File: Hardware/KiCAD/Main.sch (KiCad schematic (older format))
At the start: 4 parts

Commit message: More work on the schematic
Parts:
- added C?: C, symbol C
- added IC?: MAX3232_BJH, maxim-DIL16, symbol MAX3232_BJH
- added J?: ICSP, symbol CONN_01X06
- added J?: DB9, symbol DB9
- added JP?: Jumper, symbol Jumper
- added R?: 10K, symbol R
- added R? (x2): 220, symbol R
- added U?: POXA1328-007, symbol POXA1328-007
- added U?: 4000series-4052, DIP16, symbol 4000series-4052
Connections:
- net GND: now also J?.3 (P3), J?.5, JP?.2, U?.6 (INH)
- net PGC: now also J?.5 (P5)
- net PGD: now also J?.4 (P4)
- net RX2: now also R?.1
- net RX4: now also J?.3
- net S1: now also U?.10 (A)
- net S2: now also U?.9 (B)
- net TX2: now also R?.1
- net TX4: now also J?.2
- net ~MCLR: now reaches U?.1 (RE3/~MCLR)
- net ~MCLR: now also C?.1, J?.1 (P1), R?.2
- new net: C?.2, JP?.1
- new net: R?.2, U?.10 (RX)
- new net: R?.2, U?.9 (TX)
- new net +3.3V: J?.2 (P2), R?.1
- new net 1PPS: U?.6 (1PPS)
- new net DSR1: U?.1 (Y0)
- new net DSR2: U?.5 (Y1)
- new net DSR3: U?.2 (Y2)
- new net DSR4: U?.4 (Y3)
- new net DTR: U?.3 (Y_COM)
- new net DTR1: U?.12 (X0)
- new net DTR2: U?.14 (X1)
- new net DTR3: U?.15 (X2)
- new net DTR4: U?.11 (X3)
- new net DTS: U?.13 (X_COM)
- new net FIX: U?.5 (3D-FIX)
- no-connect marks 5 -> 12
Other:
- moved on the sheet: U?A

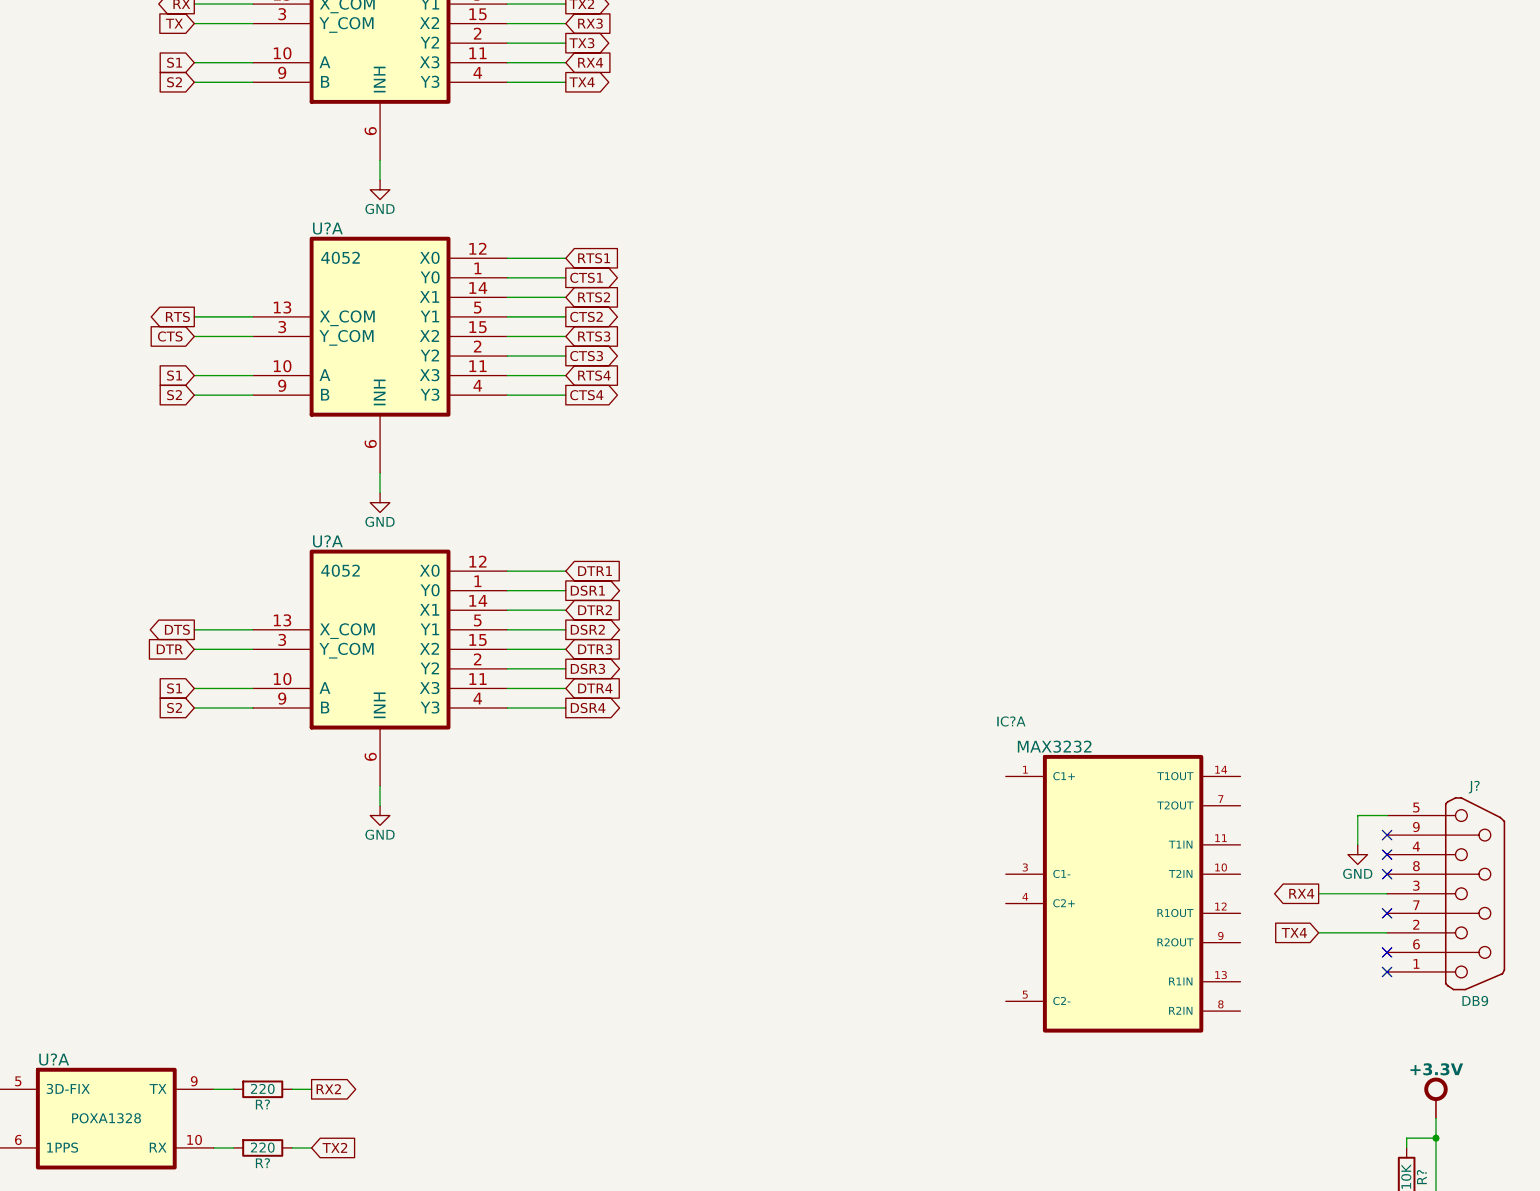
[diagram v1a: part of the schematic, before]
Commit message: Pretty much finished the RS232 side of things
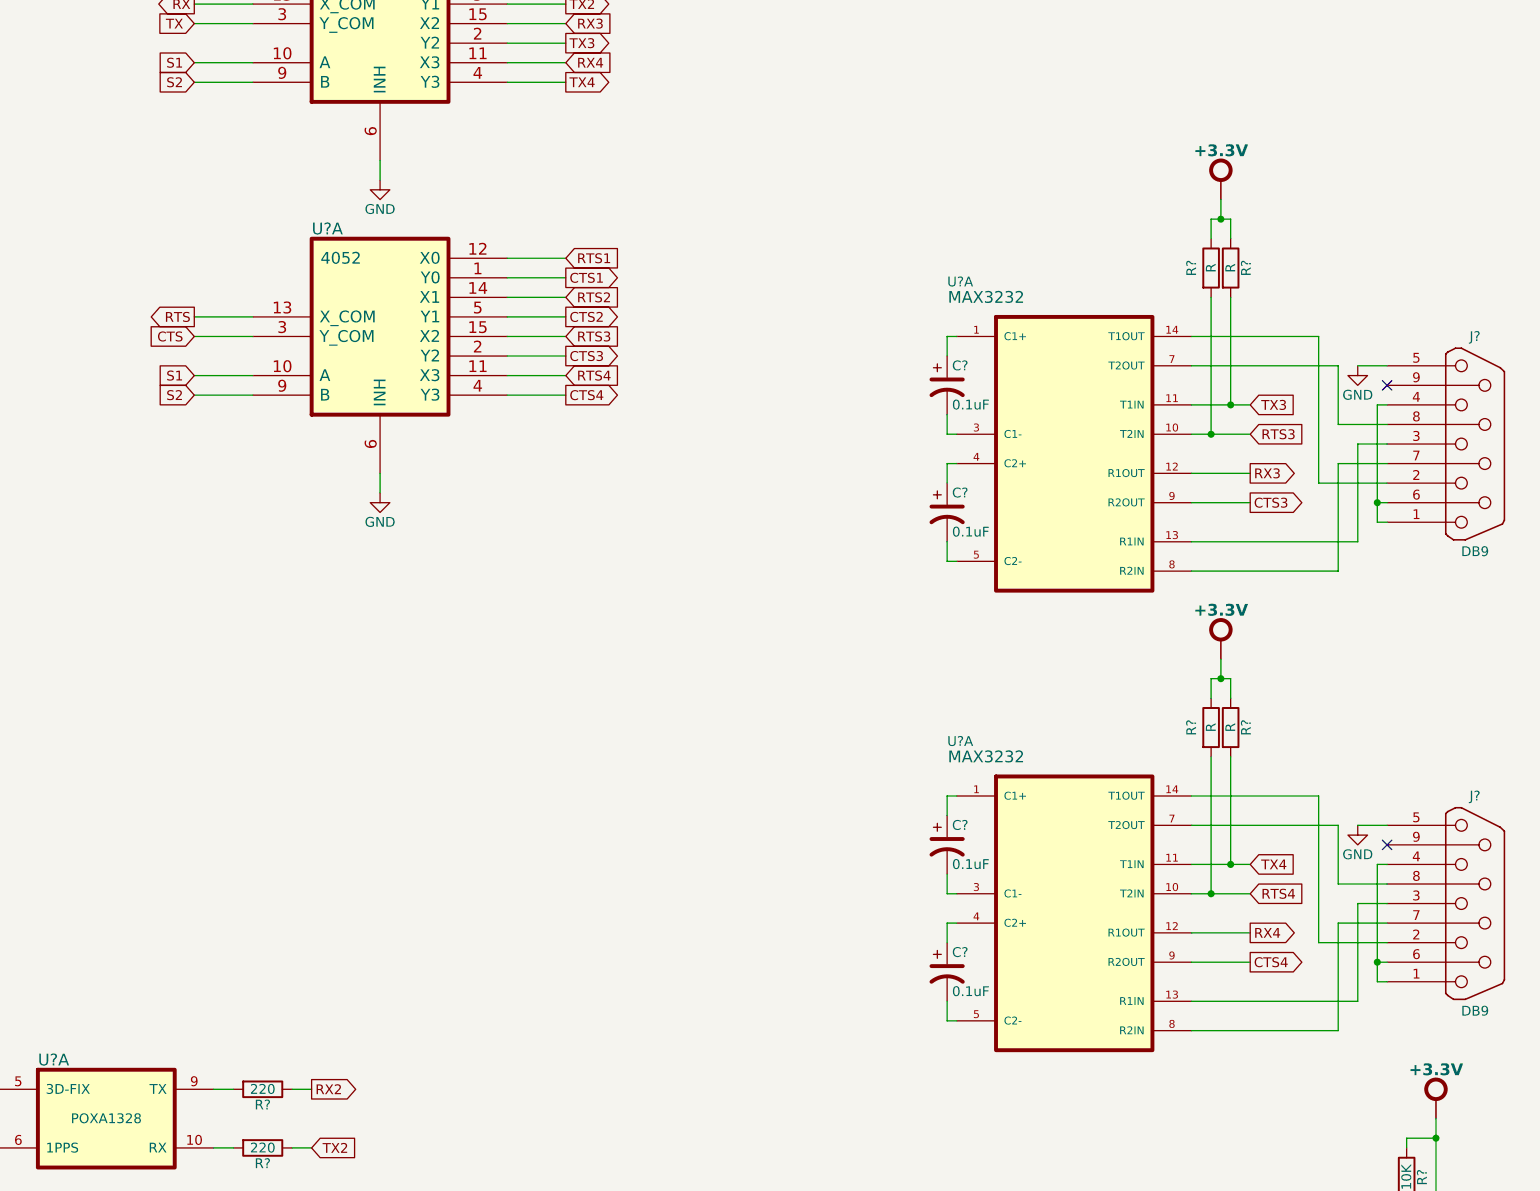
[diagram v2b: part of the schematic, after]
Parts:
- removed IC?: MAX3232_BJH, maxim-DIL16, symbol MAX3232_BJH
- removed J?: DB9, symbol DB9
- removed U?: 4000series-4052, DIP16, symbol 4000series-4052
- added C? (x4): 0.1uF, symbol CP1
- added J? (x2): DB9, symbol DB9
- added R? (x4): R, symbol R
- added U? (x2): MAX3232_BJH, maxim-DIL16, symbol MAX3232_BJH
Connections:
- net +3.3V: now also R?.1, R?.1, R?.1, R?.1
- net CTS3: now also U?.9 (R2OUT)
- net CTS4: now also U?.9 (R2OUT)
- net GND: now also J?.5, J?.5
- net RTS3: now also R?.2, U?.10 (T2IN)
- net RTS4: now also R?.2, U?.10 (T2IN)
- net RX3: now also U?.12 (R1OUT)
- net RX4: now also U?.12 (R1OUT)
- net TX3: now also R?.2, U?.11 (T1IN)
- net TX4: now also R?.2, U?.11 (T1IN)
- new net: J?.1, J?.4, J?.6 (P6) (x2)
- new net: J?.2, U?.14 (T1OUT) (x2)
- new net: J?.3, U?.13 (R1IN) (x2)
- new net: J?.7 (P7), U?.8 (R2IN) (x2)
- new net: J?.8 (P8), U?.7 (T2OUT) (x2)
- new net: C?.1, U?.1 (C1+) (x2)
- new net: C?.2, U?.3 (C1-) (x2)
- new net: C?.1, U?.4 (C2+) (x2)
- new net: C?.2, U?.5 (C2-) (x2)
- no-connect marks 12 -> 8

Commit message: More work on the schematic
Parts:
- added C?: 12pF, symbol C_Small
- added C?: 10pF, symbol C_Small
- added R?: 10K, symbol R
- added U?: MCP795XX, symbol MCP795XX
- added Y?: 32.768Hz, symbol Crystal
- added Y?: 12MHz, symbol Crystal
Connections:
- net +3.3V: now also R?.1
- net at U?.10 (RA6/OSC2/CLKout): now also Y?.2
- net SCLK: now reaches U?.14 (RC3/SCK/SCL)
- net SCLK: now also U?.8 (SCK)
- net MSDI: now reaches U?.15 (SDA/SDI/RC4)
- net MSDI: now also U?.7 (SO)
- net MSDO: now reaches U?.16 (SDO/RC5)
- net MSDO: now also U?.6 (SI)
- net RTC_SS: now reaches U?.21 (AN10/RB0)
- net RTC_SS: now also U?.3 (~CS)
- net ALARM: now reaches U?.22 (AN8/INT1/RB1)
- net ALARM: now also R?.2, U?.9 (MFP)
- net FLASH_SS: now reaches U?.26 (RB5)
- net at U?.9 (RA7/OSC1/CLKin): now also Y?.1
- new net: C?.1, U?.1 (X1), Y?.1
- new net: C?.1, U?.2 (X2), Y?.2
- new net: C?.2, C?.2
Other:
- moved on the sheet: C?, J?, JP?, R?, U?A

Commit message: more work on the schematic
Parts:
- added U?: S25FL127S_SOIC, symbol S25FL127S_SOIC
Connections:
- wire segments 166 -> 170
- no-connect marks 8 -> 11
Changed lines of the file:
@@
 LIBS:Relays
 LIBS:Transistors-BJH
+LIBS:MemoryDevices-BJH
 LIBS:ptws-cache
 EELAYER 25 0
@@
 Wire Wire Line
 	7350 5550 7350 5700
+$Comp
+L S25FL127S_SOIC U?
+U 1 1 57B9C014
+P 5850 4650
+F 0 "U?" H 5850 4700 60  0000 L CNN
+F 1 "S25FL127S_SOIC" H 5850 4800 60  0000 L CNN
+F 2 "" H 6200 4450 60  0000 C CNN
+F 3 "" H 6200 4450 60  0000 C CNN
+	1    5850 4650
+	1    0    0    -1
+$EndComp
+Text GLabel 5350 4750 0    50   Input ~ 0
+FLASH_SS
+Wire Wire Line
+	5350 4750 5650 4750
+Text GLabel 5350 4850 0    50   Input ~ 0
+SCLK
+Wire Wire Line
+	5350 4850 5650 4850
+Text GLabel 5350 5050 0    50   Input ~ 0
+MSDO
+Wire Wire Line
+	5350 5050 5650 5050
+Text GLabel 5350 4950 0    50   Output ~ 0
+MSDI
+Wire Wire Line
+	5350 4950 5650 4950
+NoConn ~ 7100 4850
+NoConn ~ 7100 4750
+NoConn ~ 7100 4950
 $EndSCHEMATC

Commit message: more work on PTWS schematic
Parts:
- U4: renamed from U?; symbol S25FL127S_SOIC -> S25FL127S_SOIC-RESCUE-ptws
- gave numbers to parts that had none: 29
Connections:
- wire segments 170 -> 171

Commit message: More work on PTWS
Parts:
- added C25, C26: C_Small, symbol C_Small
- added J4: SPARE, symbol CONN_01X02
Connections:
- net GND: now also C2.2, C3.2, C25.2, C26.1
- net at U1.10 (RA6/OSC2/CLKout), Y1.2: now also C26.2
- net at U1.24 (CANRX/INT3/RB3): now also J4.2 (P2)
- net at U1.25 (AN9/RB4): now also J4.1 (P1)
- net at U1.9 (RA7/OSC1/CLKin), Y1.1: now also C25.1
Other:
- moved on the sheet: Y1

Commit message: More work on PTWS schematic
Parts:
- removed C25, C26: C_Small, symbol C_Small
- removed J4: SPARE, symbol CONN_01X02
- removed Y1: 12MHz, symbol Crystal
- added TP?: CLK_OUT, symbol CONN_01X01
- R5, R7: value R -> 1K
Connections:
- net ACTIV_LED is gone; now on net BT_ACTIV: U3.12 (PIO3/MOSI/WS)
- net CONN_LED is gone; now on net BT_CONN: U3.10 (SCK/PIO1)
- net EVENT_LED is gone; now on net BT_MLDP_EV: U3.11 (PIO2/CS/MLDP_EV)
- net GND: now also C2.1; no longer C2.2
- net at U1.10 (RA6/OSC2/CLKout): now also TP?.1 (P1)
- net BT_MLDP_EV: now reaches U1.24 (CANRX/INT3/RB3)
- net BT_CONN: now reaches U1.25 (AN9/RB4)
- net BT_ACTIV: now reaches U1.9 (RA7/OSC1/CLKin)
- net at U7.1 (X1), Y2.1: now also C2.2; no longer C2.1
- net CTS2: no longer names the net of U6.5 (Y1)
- net MSDI renamed MISO
- net MSDO renamed MOSI
- net RTS2: no longer names the net of U6.14 (X1)
- no-connect marks 11 -> 14
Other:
- moved on the sheet: C2, C3, R2, R3, U1A, U2A, U3A, U4A, U5A, U6A

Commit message: more work on the schematic
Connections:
- no-connect marks 14 -> 13
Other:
- moved on the sheet: C2, C3
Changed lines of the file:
@@
 LIBS:Relays
 LIBS:Transistors-BJH
+LIBS:MemoryDevices-BJH
 LIBS:ptws-cache
 EELAYER 25 0
@@
 L C_Small C3
 U 1 1 57B87644
-P 7850 5950
-F 0 "C3" H 7800 6100 50  0000 L CNN
-F 1 "12pF" H 7700 6150 50  0000 L CNN
-F 2 "" H 7850 5950 50  0000 C CNN
-F 3 "" H 7850 5950 50  0000 C CNN
-	1    7850 5950
-	-1   0    0    1
-$EndComp
-$Comp
-L C_Small C2
-U 1 1 57B87717
-P 7850 5750
-F 0 "C2" V 7900 5600 50  0000 L CNN
-F 1 "10pF" V 8000 5600 50  0000 L CNN
-F 2 "" H 7850 5750 50  0000 C CNN
-F 3 "" H 7850 5750 50  0000 C CNN
-	1    7850 5750
+P 7850 6000
+F 0 "C3" H 7950 6000 50  0000 L CNN
+F 1 "12pF" H 7850 5900 50  0000 L CNN
+F 2 "" H 7850 6000 50  0000 C CNN
+F 3 "" H 7850 6000 50  0000 C CNN
+	1    7850 6000
 	-1   0    0    1
 $EndComp
@@
 L GND #PWR012
 U 1 1 58010C74
-P 7700 5950
-F 0 "#PWR012" H 7700 5700 50  0001 C CNN
-F 1 "GND" H 7700 5800 50  0000 C CNN
-F 2 "" H 7700 5950 50  0000 C CNN
-F 3 "" H 7700 5950 50  0000 C CNN
-	1    7700 5950
+P 7600 5950
+F 0 "#PWR012" H 7600 5700 50  0001 C CNN
+F 1 "GND" H 7600 5800 50  0000 C CNN
+F 2 "" H 7600 5950 50  0000 C CNN
+F 3 "" H 7600 5950 50  0000 C CNN
+	1    7600 5950
 	1    0    0    -1
 $EndComp
@@
 	9700 1400 9700 1950
 Wire Wire Line
-	9500 1950 9800 1950
-Wire Wire Line
-	9500 2100 9800 2100
+	9500 1950 9700 1950
+Wire Wire Line
+	9700 1950 9800 1950
+Wire Wire Line
+	9500 2100 9600 2100
+Wire Wire Line
+	9600 2100 9800 2100
 Wire Wire Line
 	10250 2050 10500 2050
@@
 	10450 1950 10500 1950
 Wire Wire Line
-	10450 1950 10450 2550
+	10450 1950 10450 2450
+Wire Wire Line
+	10450 2450 10450 2550
 Wire Wire Line
 	10450 2550 10500 2550
@@
 Connection ~ 1100 6350
 Wire Wire Line
-	1100 6250 1100 6850
+	1100 6250 1100 6350
+Wire Wire Line
+	1100 6350 1100 6850
 Connection ~ 950  5900
 Wire Wire Line
@@
 	950  6450 850  6450
 Wire Wire Line
-	950  5800 950  6450
+	950  5800 950  5900
+Wire Wire Line
+	950  5900 950  6450
 Wire Wire Line
 	1300 6750 850  6750
@@
 	1300 6650 850  6650
 Wire Wire Line
-	850  6350 1300 6350
+	850  6350 1100 6350
+Wire Wire Line
+	1100 6350 1300 6350
 Wire Wire Line
 	3350 3350 3700 3350
@@
 	9600 1100 9600 1000
 Wire Wire Line
-	9600 1000 9700 1000
+	9600 1000 9650 1000
+Wire Wire Line
+	9650 1000 9700 1000
 Wire Wire Line
 	9700 1000 9700 1100
@@
 	9700 3750 9700 4300
 Wire Wire Line
-	9500 4300 9800 4300
-Wire Wire Line
-	9500 4450 9800 4450
+	9500 4300 9700 4300
+Wire Wire Line
+	9700 4300 9800 4300
+Wire Wire Line
+	9500 4450 9600 4450
+Wire Wire Line
+	9600 4450 9800 4450
 Wire Wire Line
 	10250 4400 10500 4400
@@
 	10450 4300 10500 4300
 Wire Wire Line
-	10450 4300 10450 4900
+	10450 4300 10450 4800
+Wire Wire Line
+	10450 4800 10450 4900
 Wire Wire Line
 	10450 4900 10500 4900
@@
 	9600 3450 9600 3350
 Wire Wire Line
-	9600 3350 9700 3350
+	9600 3350 9650 3350
+Wire Wire Line
+	9650 3350 9700 3350
 Wire Wire Line
 	9700 3350 9700 3450
@@
 	9950 5750 9650 5750
 Wire Wire Line
-	7200 6200 8250 6200
+	7200 6200 7350 6200
+Wire Wire Line
+	7350 6200 8250 6200
 Wire Wire Line
 	9950 6000 9650 6000
@@
 	9950 6200 9650 6200
 Wire Wire Line
-	8050 5700 8050 5650
-Wire Wire Line
-	8250 5650 8250 5750
-Wire Wire Line
-	8050 6000 8050 6050
-Wire Wire Line
-	8250 6050 8250 5950
-Connection ~ 8050 5650
-Connection ~ 8050 6050
+	8050 5700 8050 5600
+Wire Wire Line
+	8250 5600 8250 5750
+Wire Wire Line
+	8050 6000 8050 6100
+Wire Wire Line
+	8250 6100 8250 5950
+Connection ~ 8050 5600
+Connection ~ 8050 6100
 Wire Wire Line
 	4300 1800 4050 1800
@@
 	4300 1700 4050 1700
 Wire Wire Line
-	7700 5950 7700 5850
+	7600 5950 7600 5850
 Wire Wire Line
 	4050 1600 4300 1600
 Wire Wire Line
-	7850 5650 8250 5650
-Wire Wire Line
-	7850 6050 8250 6050
-Wire Wire Line
-	7700 5850 7850 5850
+	7850 5600 8050 5600
+Wire Wire Line
+	8050 5600 8250 5600
+Wire Wire Line
+	7850 6100 8050 6100
+Wire Wire Line
+	8050 6100 8250 6100
 Text GLabel 4300 1600 2    50   Input ~ 0
 BT_MLDP_EV
@@
 NoConn ~ 7000 3000
 NoConn ~ 7000 3100
-NoConn ~ 7150 5400
+$Comp
+L C_Small C2
+U 1 1 57B87717
+P 7850 5700
+F 0 "C2" H 7950 5700 50  0000 L CNN
+F 1 "10pF" H 7850 5600 50  0000 L CNN
+F 2 "" H 7850 5700 50  0000 C CNN
+F 3 "" H 7850 5700 50  0000 C CNN
+	1    7850 5700
+	-1   0    0    1
+$EndComp
+Wire Wire Line
+	7850 5800 7850 5850
+Wire Wire Line
+	7850 5850 7850 5900
+Wire Wire Line
+	7600 5850 7850 5850
+Connection ~ 7850 5850
 $EndSCHEMATC
